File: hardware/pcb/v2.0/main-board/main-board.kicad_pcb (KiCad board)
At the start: 4 copper layers, 102 x 33 mm, 140 parts, among them J1 USB_C_Receptacle_USB2.0_16P, Q1 AO3401A, Q2 AO3401A, Q3 AO3400A, Q4 AO3401A, Q5 AO3401A, Q6 AO3401A, Q7 AO3400A, Q8 AO3401A, Q9 AO3401A, U1 TL431DBZ, U2 ESP32-S2-WROVER-I, U3 BH1750FVI-TR, U4 BH1750FVI-TR, U5 AP2112K-3.3, U6 TP4056, U7 FS312MH

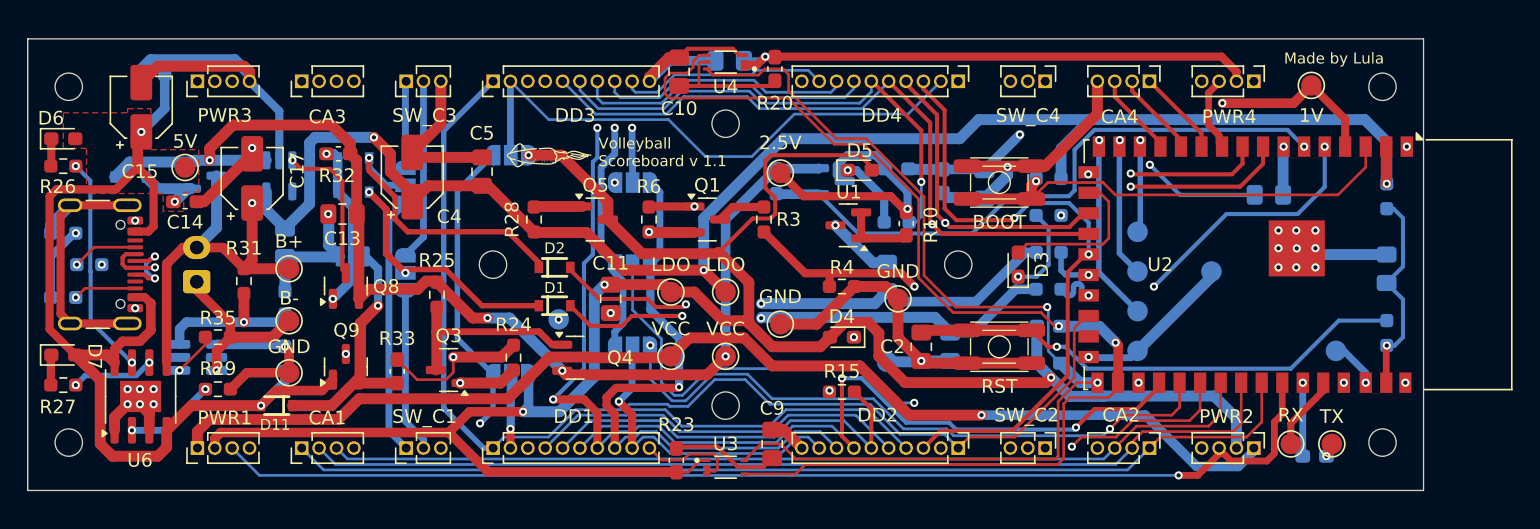
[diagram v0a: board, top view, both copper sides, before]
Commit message: added docs and v2 of the main pcb is about done
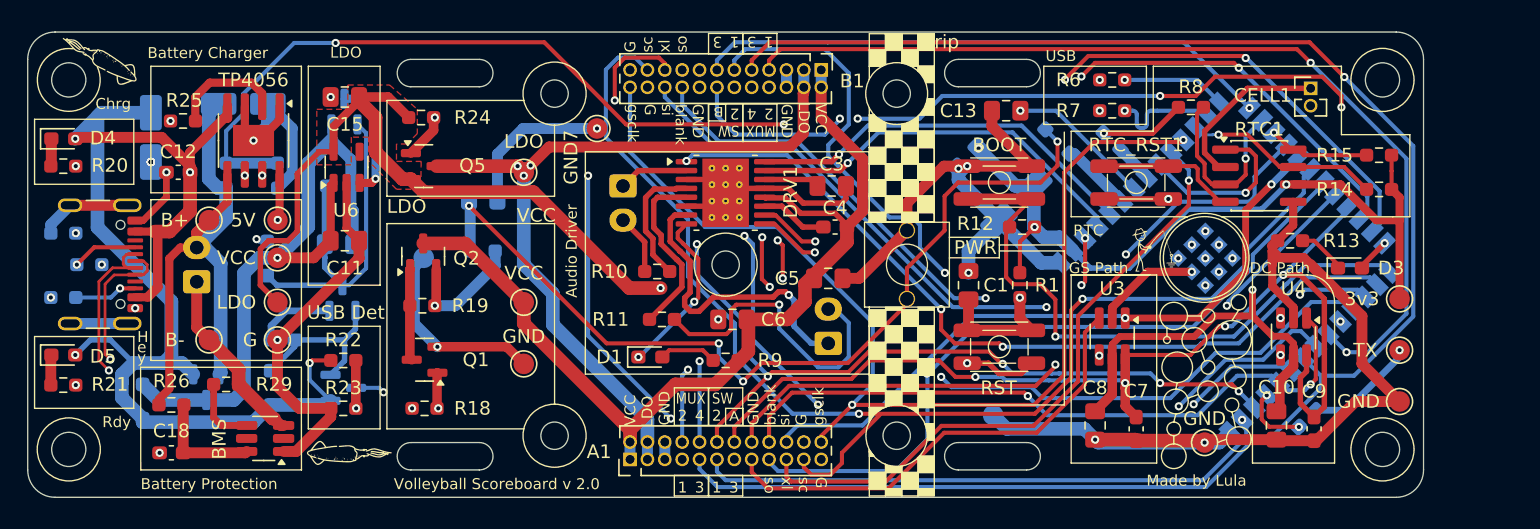
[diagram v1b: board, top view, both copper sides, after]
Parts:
- removed 11, 12, 13, 1V, 2.5V, 46, RX: TestPoint_Alt, TestPoint:TestPoint_Pad_D1.5mm
- removed AB_1, AB_2, AB_3, ALT_A1, ALT_B1, SW_1, SW_2: SolderJumper_3_Open, Jumper:SolderJumper-3_P1.3mm_Open_RoundedPad1.0x1.5mm_NumberLabels
- removed the C11 at (91.6, 102.5)
- removed the C12 at (100.3, 85.1)
- removed CA1, CA2, CA3, CA4, PWR1, PWR2, PWR3, PWR4: Conn_01x04_Pin, Connector_PinHeader_1.27mm:PinHeader_1x04_P1.27mm_Vertical
- removed D10: BAT20JFILM, BAT20JFILM:SOD-323
- removed D11, D9: BAT20J, BAT20JFILM:SOD-323
- removed the D4 at (108.5, 105.3)
- removed the D5 at (109.8, 93.1)
- removed DD1, DD2, DD3, DD4: Conn_01x10_Pin, Connector_PinHeader_1.27mm:PinHeader_1x10_P1.27mm_Vertical
- removed the GND at (68.1, 107.9)
- removed the GND at (112.6, 102.5)
- removed the GND at (104.0, 104.3)
- removed the GND at (130.1, 106.3)
- removed the GND at (87.8, 104.0)
- removed the GND at (135.5, 100.5)
- removed the GND at (111.8, 107.1)
- removed the LDO at (96.0, 102.0)
- removed the LDO at (100.0, 102.0)
- removed the Q1 at (98.7, 96.7)
- removed the Q2 at (107.8, 93.9)
- removed the R12 at (103.7, 93.9)
- removed the R16 at (112.5, 96.9)
- removed the R20 at (103.6, 85.7)
- removed the R21 at (123.6, 107.2)
- removed the R23 at (96.4, 114.3)
- removed R34: 1M, Resistor_SMD:R_0603_1608Metric_Pad0.98x0.95mm_HandSolder
- removed the R5 at (148.3, 105.0)
- removed the R6 at (94.4, 96.7)
- removed SW_C1, SW_C2, SW_C3, SW_C4: Conn_01x03_Pin, Connector_PinHeader_1.27mm:PinHeader_1x03_P1.27mm_Vertical
- removed U2: ESP32-S2-WROVER-I, RF_Module:ESP32-S2-WROVER
- removed the VCC at (96.0, 106.7)
- removed the VCC at (100.0, 106.7)
- added 3v3: TestPoint_Alt, TestPoint:TestPoint_Pad_D1.5mm, F.Cu at (149.2, 102.5)
- added A1: Conn_02x12_Odd_Even, Connector_PinHeader_1.27mm:PinHeader_2x12_P1.27mm_Vertical, F.Cu at (93.0, 114.2)
- added B1: Conn_02x12_Odd_Even, Connector_PinHeader_1.27mm:PinHeader_2x12_P1.27mm_Vertical, F.Cu at (107.0, 85.8)
- added BUZZER A1: Conn_01x02_Pin, Connector_JST:JST_XH_B2B-XH-A_1x02_P2.50mm_Vertical, B.Cu at (92.5, 94.2)
- added BUZZER B1: Conn_01x02_Pin, Connector_JST:JST_XH_B2B-XH-A_1x02_P2.50mm_Vertical, B.Cu at (107.5, 105.8)
- added C17: 0.1uF, Capacitor_SMD:C_0805_2012Metric_Pad1.18x1.45mm_HandSolder, B.Cu at (71.8, 98.5)
- added C21: 100nF, Capacitor_SMD:C_0805_2012Metric_Pad1.18x1.45mm_HandSolder, B.Cu at (82.3, 95.2)
- added C3: 2.2uF, Capacitor_SMD:C_0805_2012Metric_Pad1.18x1.45mm_HandSolder, F.Cu at (107.8, 94.2)
- added C4: 10nF, Capacitor_SMD:C_0603_1608Metric_Pad1.08x0.95mm_HandSolder, F.Cu at (108.0, 97.2)
- added C5: 10uF, Capacitor_SMD:C_0805_2012Metric_Pad1.18x1.45mm_HandSolder, F.Cu at (107.5, 101.0)
- added CELL1: Conn_01x02_Pin, Connector_PinHeader_1.27mm:PinHeader_1x02_P1.27mm_Vertical, F.Cu at (142.8, 87.1)
- added D6: BAT20J, Diode_SMD:D_SOD-323_HandSoldering, B.Cu at (57.4, 110.0)
- added D7: BAT20J, Diode_SMD:D_SOD-323_HandSoldering, B.Cu at (66.5, 99.5)
- added DRV1: DRV8833PWP, Package_SO:HTSSOP-16-1EP_4.4x5mm_P0.65mm_EP3.4x5mm_Mask2.46x2.31mm_ThermalVias, F.Cu at (100.0, 94.8)
- added G: TestPoint_Alt, TestPoint:TestPoint_Pad_D1.5mm, F.Cu at (67.2, 105.5)
- added G***: LOGO, Luis:lula1, F.Cu at (54.2, 85.0)
- added G***: LOGO, Luis:fishing, F.Cu at (131.2, 99.0)
- added G***: LOGO, Luis:rake, B.Cu at (101.5, 94.8)
- added GND: TestPoint_Alt, TestPoint:TestPoint_Pad_D1.5mm, F.Cu at (149.2, 110.0)
- added GND: TestPoint_Alt, TestPoint:TestPoint_Pad_D1.5mm, F.Cu at (85.2, 107.2)
- added GND: TestPoint_Alt, TestPoint:TestPoint_Pad_D1.5mm, F.Cu at (135.0, 113.0)
- added GND3: TestPoint_Alt, TestPoint:TestPoint_Pad_D1.5mm, B.Cu at (77.9, 99.5)
- added GND4: TestPoint_Alt, TestPoint:TestPoint_Pad_D1.5mm, B.Cu at (119.5, 111.0)
- added GND7: TestPoint_Alt, TestPoint:TestPoint_Pad_D1.5mm, F.Cu at (90.6, 90.0)
- added H4: MountingHole, MountingHole:MountingHole_2mm, F.Cu at (87.5, 87.5)
- added LDO: TestPoint_Alt, TestPoint:TestPoint_Pad_D1.5mm, F.Cu at (85.2, 93.2)
- added LDO: TestPoint_Alt, TestPoint:TestPoint_Pad_D1.5mm, F.Cu at (67.2, 102.8)
- added PWR: SW_Push, Luis:Kahil Mute 6.2x6.2x7.3, F.Cu at (113.2, 100.0)
- added R11: 300, Resistor_SMD:R_0603_1608Metric_Pad0.98x0.95mm_HandSolder, F.Cu at (95.3, 104.0)
- added R30: 10k, Resistor_SMD:R_0603_1608Metric_Pad0.98x0.95mm_HandSolder, B.Cu at (82.2, 99.0)
- added R8: 100k, Resistor_SMD:R_0603_1608Metric_Pad0.98x0.95mm_HandSolder, F.Cu at (134.0, 88.5)
- added RTC1: DS3231MZ, Package_SO:SOIC-8_3.9x4.9mm_P1.27mm, F.Cu at (139.0, 93.5)
- added RTC_RST1: SW_Push, Luis:Button_3x4x2.5, F.Cu at (130.0, 94.0)
- added VCC: TestPoint_Alt, TestPoint:TestPoint_Pad_D1.5mm, F.Cu at (85.2, 102.8)
- added VCC: TestPoint_Alt, TestPoint:TestPoint_Pad_D1.5mm, F.Cu at (67.2, 99.5)
- BMS: renamed from U7; moved to F.Cu
- C1: value 1uF -> 100nF; moved to F.Cu
- C13: renamed from C3; moved to F.Cu
- C14: renamed from C15; moved to B.Cu
- C15: renamed from C16; moved to F.Cu
- C16: renamed from C17; moved to B.Cu
- C18, C6, R9: moved to F.Cu
- C19: renamed from C4; moved to B.Cu
- C2: value 0.1uF -> 1nF; footprint Capacitor_SMD:C_0805_2012Metric_Pad1.18x1.45mm_HandSolder -> Capacitor_SMD:C_0603_1608Metric_Pad1.08x0.95mm_HandSolder; moved to B.Cu
- C20: renamed from C5; moved to B.Cu
- C7: value C -> 1nF; footprint Capacitor_SMD:C_0805_2012Metric_Pad1.18x1.45mm_HandSolder -> Capacitor_SMD:C_0603_1608Metric_Pad1.08x0.95mm_HandSolder; moved to F.Cu
- C8: value C -> 0.1uF; moved to F.Cu
- C9: value 0.1uF -> 1nF; footprint Capacitor_SMD:C_0805_2012Metric_Pad1.18x1.45mm_HandSolder -> Capacitor_SMD:C_0603_1608Metric_Pad1.08x0.95mm_HandSolder
- D1: value BAT20JFILM -> LED; footprint BAT20JFILM:SOD-323 -> LED_SMD:LED_0603_1608Metric_Pad1.05x0.95mm_HandSolder
- D2: value BAT20JFILM -> BAT20J; footprint BAT20JFILM:SOD-323 -> Diode_SMD:D_SOD-323_HandSoldering; moved to B.Cu
- D8: footprint BAT20JFILM:SOD-323 -> Diode_SMD:D_SOD-323_HandSoldering
- Q6: renamed from Q8; moved to B.Cu
- Q7: renamed from Q9; moved to B.Cu
- R1: renamed from R2; moved to F.Cu
- R10: value R -> 300; footprint Capacitor_SMD:C_0603_1608Metric_Pad1.08x0.95mm_HandSolder -> Resistor_SMD:R_0603_1608Metric_Pad0.98x0.95mm_HandSolder
- R12: renamed from R11; moved to F.Cu
- R13: value R -> 2.2K; footprint Capacitor_SMD:C_0603_1608Metric_Pad1.08x0.95mm_HandSolder -> Resistor_SMD:R_0603_1608Metric_Pad0.98x0.95mm_HandSolder; moved to F.Cu
- R14: value R -> 4.7k; footprint Capacitor_SMD:C_0603_1608Metric_Pad1.08x0.95mm_HandSolder -> Resistor_SMD:R_0603_1608Metric_Pad0.98x0.95mm_HandSolder; moved to F.Cu
- R15: value 2.2K -> 4.7k
- R16: renamed from R3; value R -> 100k; moved to B.Cu
- R17: renamed from R4; value R -> 100k; moved to B.Cu
- R18: renamed from R24; value 1M -> 100k
- R19: renamed from R25; value 1M -> 100k
- R22: value 4.7k -> 56k; footprint Capacitor_SMD:C_0603_1608Metric_Pad1.08x0.95mm_HandSolder -> Resistor_SMD:R_0603_1608Metric_Pad0.98x0.95mm_HandSolder; moved to F.Cu
- R23: renamed from R30; value 10K -> 100k; moved to F.Cu
- R24: renamed from R28; value 1M -> 100k
- R27: renamed from R33; value 1M -> 100k; moved to B.Cu
- R28: renamed from R32; value 1M -> 100k; moved to B.Cu
- R6: renamed from R18; moved to F.Cu
- R7: renamed from R17; moved to F.Cu
- U1: value TL431DBZ -> ESP32-S3-WROOM-1; footprint Package_TO_SOT_SMD:SOT-23 -> Luis:ESP32-S3-WROOM-1U; moved to B.Cu
- U3, U4: value BH1750FVI-TR -> 74LVC1G3157; footprint BH1750FVI-TR:XDCR_BH1750FVI-TR -> Package_TO_SOT_SMD:SOT-23-6_Handsoldering
- U6: renamed from U5; moved to F.Cu
- moved R22 51.6 mm to (72.1, 107.0), turned to 0 degrees
- moved C10 50.7 mm to (140.2, 111.8), turned to 90 degrees
- moved U4 46.1 mm to (141.5, 105.2), turned to -90 degrees
- moved C19 44.2 mm to (121.2, 95.5), turned to -135 degrees
- moved R15 42.9 mm to (147.8, 92.0), turned to 0 degrees
- moved R17 42.0 mm to (67.2, 93.5), turned to -90 degrees
- moved C9 39.6 mm to (143.0, 112.0)
- moved R16 39.4 mm to (63.5, 93.5), turned to 90 degrees
- moved D2 37.9 mm to (124.2, 91.0), turned to -45 degrees
- moved C20 35.6 mm to (117.8, 92.2), turned to 45 degrees
- moved R14 31.9 mm to (147.8, 94.5), turned to 0 degrees
- moved C1 30.6 mm to (117.8, 101.5)
- moved U3 29.8 mm to (128.2, 105.2), turned to -90 degrees
- moved R13 29.2 mm to (141.2, 98.2), turned to 180 degrees
- moved R23 28.1 mm to (72.1, 110.5)
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- renumbered C13 to C11, C14 to C12, D6 to D4, D7 to D5, J1 to J6, Q3 to Q1, Q4 to Q2, Q6 to Q3, Q7 to Q4, R1 to R2, R26 to R20, R27 to R21, R29 to R25, R31 to R26, R35 to R29, R7 to R3, R8 to R4, R19 to R5, U6 to TP4056
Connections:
- BOOT pad 2: Net-(U2-IO00) -> Net-(U1-GPIO0/BOOT)
- C10 pad 2: Net-(U4-DVI) -> LDO_CTRL
- C13 pad 1: /ADC_BAT_EN -> GND
- C13 pad 2: Net-(Q1-G) -> /ADC_BAT
- C2 pad 2: Net-(C2-Pad2) -> Net-(U1-GPIO15/U0RTS/ADC2_CH4/XTAL_32K_P)
- C6 pad 1: /1V -> GND
- C6 pad 2: GND -> VCC_CTRL
- C7 pad 1: /USB_D- -> /SLOT_A_DET
- C8 pad 1: /USB_D+ -> GND
- C8 pad 2: GND -> LDO_CTRL
- C9 pad 1: GND -> /SLOT_A_DET
- C9 pad 2: Net-(U3-DVI) -> GND
- Q2 pad 3: /VCC_CTRL -> VCC_CTRL
- Q3 pad 2: VCC -> +BATT
- Q3 pad 3: +BATT -> VCC
- Q4 pad 1: Net-(Q7-G) -> Net-(D8-K)
- Q4 pad 3: Net-(Q7-D) -> Net-(D7-A)
- Q6 pad 1: Net-(Q7-D) -> Net-(D7-A)
- Q7 pad 2: Net-(Q7-G) -> Net-(D8-K)
- R10 pad 1: /2.5V -> Net-(DRV1-AOUT2)
- R10 pad 2: Net-(U1-K) -> /BUZZER_A_-
- R12 pad 2: Net-(U2-IO00) -> Net-(U1-GPIO0/BOOT)
- R13 pad 1: /2.5V -> Net-(D3-K)
- R13 pad 2: /1V -> GND
- R14 pad 1: GND -> /RTC_SDA
- R14 pad 2: /1V -> LDO
- R15 pad 1: /XERR_A -> /RTC_SCL
- R15 pad 2: Net-(D4-K) (its old number) -> LDO
- R16 pad 1: Net-(Q1-D) (its old number) -> +BATT
- R16 pad 2: /ADC_BAT_V -> /ADC_BAT
- R17 pad 1: /ADC_BAT_V -> /ADC_BAT
- R22 pad 1: /SDA -> VBUS
- R22 pad 2: LDO_CTRL -> /VBUS_DET
- R23 pad 1: VBUS -> /VBUS_DET
- R27 pad 1: Net-(Q7-G) -> Net-(D8-K)
- R28 pad 2: Net-(Q7-D) -> Net-(D7-A)
- R5 pad 1: Net-(U2-TXD0) -> Net-(U1-U0TXD/GPIO43/CLK_OUT1)
- R6 pad 1: Net-(U2-USB_D-) -> Net-(U1-GPIO20/U1CTS/ADC2_CH9/CLK_OUT1/USB_D+)
- R7 pad 1: Net-(U2-USB_D+) -> Net-(U1-GPIO19/U1RTS/ADC2_CH8/CLK_OUT2/USB_D-)
- R9 pad 1: Net-(D3-K) -> VCC_CTRL
- R9 pad 2: GND -> Net-(D1-A)
- RST pad 1: Net-(C2-Pad2) -> /EN
- U1 pad 1: Net-(U1-K) -> GND
- U1 pad 2: Net-(U1-K) -> LDO
- U1 pad 3: GND -> /EN
- U3 pad 1: LDO_CTRL -> /GSSIN
- U3 pad 3: GND -> /GSSOUT_A
- U3 pad 4: /SDA -> /GSSIN_B
- U3 pad 5: Net-(U3-DVI) -> LDO_CTRL
- U3 pad 6: /SCL -> /SLOT_A_DET
- U4 pad 1: LDO_CTRL -> /DCSIN
- U4 pad 2: LDO_CTRL -> GND
- U4 pad 3: GND -> /DCSOUT_A
- U4 pad 4: /SDA -> /DCSIN_B
- U4 pad 5: Net-(U4-DVI) -> LDO_CTRL
- U4 pad 6: /SCL -> /SLOT_A_DET
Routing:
- net /VCC_CTRL: track 148.8 -> 0.00 mm, vias 1 -> 0
- net /MUX_3: track 0.00 -> 126.1 mm, vias 0 -> 1
- net LDO_CTRL: track 260.9 -> 136.5 mm, vias 5 -> 4
- net /MUX_1: track 0.00 -> 124.0 mm, vias 0 -> 2
- net /VPRG: track 122.7 -> 0.00 mm
- net /SW_3: track 0.00 -> 109.2 mm, vias 0 -> 1
- net /SW_1: track 0.00 -> 100.5 mm, vias 0 -> 2
- net /XLAT: track 94.5 -> 0.00 mm, vias 1 -> 0
- net /CTRL: track 94.0 -> 0.00 mm, vias 2 -> 0
- net /GSLAT: track 0.00 -> 93.7 mm, vias 0 -> 4
- net /VBUS_DET: track 0.00 -> 85.3 mm, vias 0 -> 2
- net /SDA: track 84.5 -> 0.00 mm, vias 2 -> 0
- net /BUZZER_A: track 84.2 -> 0.00 mm, vias 1 -> 0
- net /SW_PWR: track 0.00 -> 83.1 mm, vias 0 -> 5
- net /LDO_CTRL_EN: track 3.54 -> 86.3 mm, vias 0 -> 2
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- added copper zone on F.Cu, net LDO
- removed copper zone on F.Cu, net VBUS
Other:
- board size 102 x 33 mm -> 102 x 34 mm
- board text added: "1"
- board text added: "2"
- board text added: "24.5mm"
- board text added: "3"
- board text added: "4"
- board text added: "A"
- board text added: "Audio Driver"
- board text added: "B"
- board text added: "BAT"
- board text added: "Battery Charger"
- board text added: "Battery Protection"
- board text added: "Chrg"
- board text added: "DC Path"
- board text added: "G"
- board text added: "GND"
- board text added: "GS Path"
- board text added: "H"
- board text added: "LDO"
- board text added: "MUX"
- board text added: "Power Switch"
- board text added: "RTC"
- board text added: "Rdy"
- board text added: "SW"
- board text added: "USB"
- board text added: "USB Det"
- board text added: "VCC"
- board text added: "Vcc"
- board text added: "Volleyball Scoreboard v 2.0"
- board text added: "blank"
- board text added: "e"
- board text added: "gsclk"
- board text added: "rip"
- board text added: "sc"
- board text added: "si"
- board text added: "so"
- board text added: "xl"
- board text added: "y"
- board text removed: "Volleyball Scoreboard v 1.1"

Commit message: v2.0 of the main and display board is ready and in production
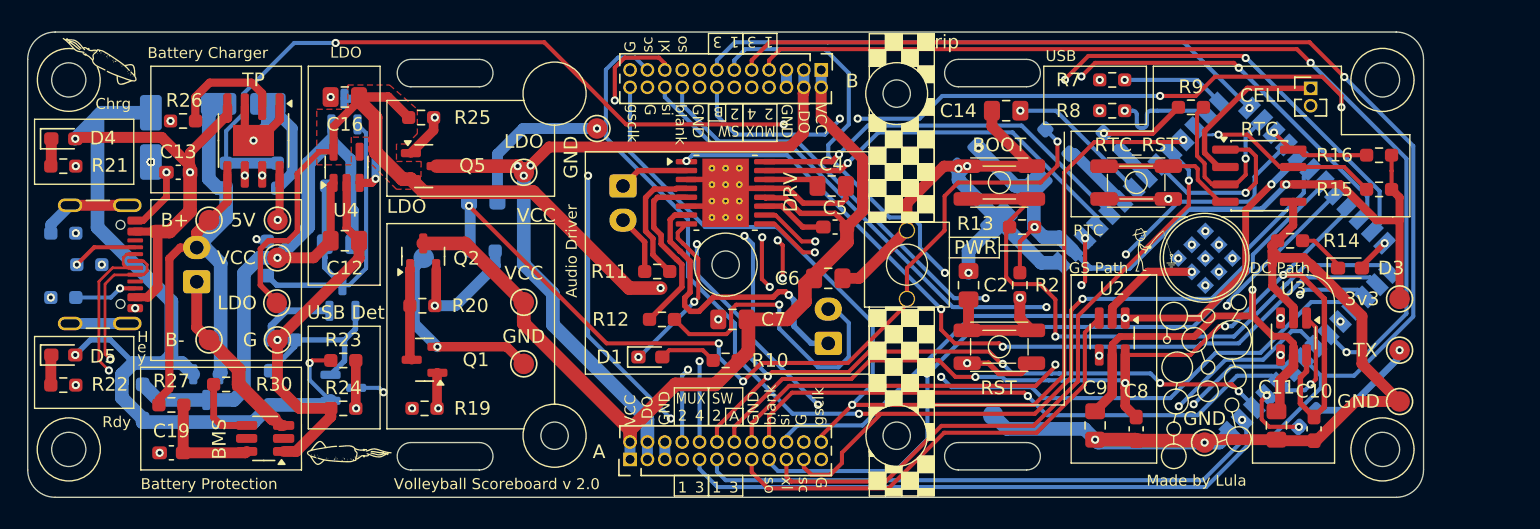
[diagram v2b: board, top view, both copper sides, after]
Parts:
- removed the H4 at (87.5, 87.5)
- BUZZER A: renamed from BUZZER A1
- BUZZER B: renamed from BUZZER B1
- moved LDO 0.07 mm to (67.2, 102.8)
- renumbered A1 to A, B1 to B, BAT1 to BAT, C21 to C1, C9 to C10, C10 to C11, C11 to C12, C12 to C13, C13 to C14, C14 to C15, C15 to C16, C16 to C17, C17 to C18, C18 to C19, C1 to C2, C19 to C20, C20 to C21, C2 to C3, C3 to C4, C4 to C5, C5 to C6, C6 to C7, C7 to C8, C8 to C9, CELL1 to CELL, DRV1 to DRV, U1 to ESP32, GND7 to GND, GND4 to GND, GND3 to GND, J6 to J1, R30 to R1, R9 to R10, R10 to R11, R11 to R12, R12 to R13, R13 to R14, R14 to R15, R15 to R16, R16 to R17, R17 to R18, R18 to R19, R1 to R2, R19 to R20, R20 to R21, R21 to R22, R22 to R23, R23 to R24, R24 to R25, R25 to R26, R26 to R27, R27 to R28, R28 to R29, R2 to R3, R29 to R30, R3 to R4, R4 to R5, R5 to R6, R6 to R7, R7 to R8, R8 to R9, RTC1 to RTC, RTC_RST1 to RTC_RST, TP4056 to TP, U3 to U2, U4 to U3, U6 to U4
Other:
- board text added: "ADC"
- board text removed: "BAT"
